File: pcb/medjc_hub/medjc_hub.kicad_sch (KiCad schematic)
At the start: 4 parts, among them J1 Barrel_Jack_Switch, U1 ESP32-C3_SUPERMINI, U2 MCP3208-CI_P, U3 NJM2747D

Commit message: 🚧 WIP: Kicad 回路図を更新
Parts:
- removed J1: Barrel_Jack_Switch, symbol Connector:Barrel_Jack_Switch
- removed U1: ESP32-C3_SUPERMINI, ESP32-C3_SUPERMINI:MODULE_ESP32-C3_SUPERMINI, symbol ESP32-C3_SUPERMINI:ESP32-C3_SUPERMINI
- added C1: 47μF, symbol Device:C_Polarized
- added C10, C12, C13, C14, C15, C4, C5, C6, C7, C8, C9: 0.1μF, symbol Device:C
- added C11, C2, C3: 0.47μF, symbol Device:C
- added D1: 1N4007, symbol Device:D
- added J1: Barrel_Jack, symbol Connector:Barrel_Jack
- added J2: Conn_01x02_Pin, Connector_PinHeader_2.54mm:PinHeader_1x02_P2.54mm_Vertical, symbol Connector:Conn_01x02_Pin
- added R1, R15, R2: 33kΩ, symbol Device:R
- added R10, R11, R12, R13, R14, R4, R5, R6, R7, R8, R9: 10kΩ, symbol Device:R
- added R3: 10kΩ, Resistor_THT:R_Box_L13.0mm_W4.0mm_P9.00mm, symbol Device:R
- added U1: NJU7223F33, symbol NJU7223F33:NJU7223F33
- added U3: ESP32-C3_SUPERMINI, ESP32-C3_SUPERMINI:MODULE_ESP32-C3_SUPERMINI, symbol ESP32-C3_SUPERMINI:ESP32-C3_SUPERMINI
- added U5, U6, U7: MERB-09, symbol MEDJC09:MERB-09
- renumbered U3 to U2, U2 to U4
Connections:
- net at U2.1 (OUT_A): now also R5.2, R6.2
- net at U2.10 (+IN_C): now also R11.1
- net GND: now reaches U2.11 (GND)
- net GND: now also U4.14 (AGND), U4.9 (DGND), C1.2, C10.2, C12.2, C13.2, C14.2, C15.2, C4.1, C5.2, C6.1, C7.2, C8.2, C9.1, J1.2, R1.1, R15.1, R2.2, U1.3 (GND), U3.G (GND), U5.3 (GND), U6.3 (GND), U7.3 (GND)
- net at U2.2 (-IN_A): now also R3.2, R6.1
- net at U2.3 (+IN_A): now also R9.2
- net +3V3: now reaches U2.4 (+Vin)
- net +3V3: now also U4.15 (VREF), U4.16 (VDD), U4.7 (CH6), C12.1, C13.1, C14.1, C15.1, C8.1, D1.1 (K), J2.2 (Pin_2), R10.2, R11.2, R9.1, U5.1 (Vs), U6.1 (Vs), U7.1 (Vs)
- net at U2.5 (+IN_B): now also R10.1
- net at U2.6 (-IN_B): now also R4.2, R7.1
- net at U2.7 (OUT_B): now also R7.2, R8.2
- net at U2.8 (OUT_C): now also R12.1, R13.1
- net at U2.9 (-IN_C): now also R13.2, R14.1
- net FME1: now reaches U4.1 (CH0)
- net FME1: now also C3.1, R1.2
- net SS: now reaches U4.10 (~CS/SHDN)
- net SS: now also U3.9 (GPIO9)
- net MOSI: now reaches U4.11 (DIN)
- net MOSI: now also U3.8 (GPIO8)
- net MISO: now reaches U4.12 (DOUT)
- net MISO: now also U3.7 (GPIO7)
- net SCK: now reaches U4.13 (CLK)
- net SCK: now also U3.4 (GPIO4)
- net SME1: now reaches U4.2 (CH1)
- net SME1: now also U5.5 (SME)
- net FME2: now reaches U4.3 (CH2)
- net FME2: now also C2.1, R2.1
- net SME2: now reaches U4.4 (CH3)
- net SME2: now also U6.5 (SME)
- net FME3: now reaches U4.5 (CH4)
- net FME3: now also C11.2, R15.2
- net SME3: now reaches U4.6 (CH5)
- net SME3: now also U7.5 (SME)
- new net: C10.1, J2.1 (Pin_1), U3.3.3 (3V3)
- new net: C1.1, C5.1, J1.1, U1.2 (Vin)
- new net: C2.2, C7.1, R8.1
- new net: C3.2, C6.2, R5.1
- new net: C4.2, D1.2 (A), U1.1 (Vout)
- new net: C11.1, C9.2, R12.2
- new net RAWME1: R3.1, U5.2 (ME)
- new net RAWME2: R4.1, U6.2 (ME)
- new net RAWME3: R14.2, U7.2 (ME)
- no-connect marks 0 -> 17
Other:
- moved on the sheet: U2, U4

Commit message: 📝 Update: 回路図を更新
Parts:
- removed C1: 47μF, symbol Device:C_Polarized
- removed C4: 0.1μF, symbol Device:C
- removed R10, R11, R9: 10kΩ, symbol Device:R
- removed U1: NJU7223F33, symbol NJU7223F33:NJU7223F33
- added C12, C6: 0.1μF, Capacitor_THT:C_Disc_D3.0mm_W2.0mm_P2.50mm, symbol Device:C
- added C4: 47μF, Capacitor_THT:CP_Radial_D5.0mm_P2.50mm, symbol Device:C_Polarized
- added J2, J3, J4: Conn_01x05_Socket, Connector_PinSocket_2.54mm:PinSocket_1x05_P2.54mm_Vertical, symbol Connector:Conn_01x05_Socket
- added J6, J7, J8: Conn_01x05_Pin, symbol Connector:Conn_01x05_Pin
- added R5: 10kΩ, Resistor_THT:R_Axial_DIN0207_L6.3mm_D2.5mm_P10.16mm_Horizontal, symbol Device:R
- added RV1: 5kΩ, GF063:GF063P, symbol Device:R_Potentiometer
- added U2: BA033CC0T, BA033CC0T:BA033CC0T, symbol BA033CC0T:BA033CC0T
- C1: renamed from C13; footprint (none) -> Capacitor_THT:C_Disc_D3.0mm_W2.0mm_P2.50mm
- C10: renamed from C6; value 0.1μF -> 1μF; footprint (none) -> Capacitor_THT:C_Disc_D3.0mm_W2.0mm_P2.50mm
- C11: renamed from C7; value 0.1μF -> 1μF; footprint (none) -> Capacitor_THT:C_Disc_D3.0mm_W2.0mm_P2.50mm
- C13: renamed from C8; footprint (none) -> Capacitor_THT:C_Disc_D3.0mm_W2.0mm_P2.50mm
- C14: renamed from C12; footprint (none) -> Capacitor_THT:C_Disc_D3.0mm_W2.0mm_P2.50mm
- C15: renamed from C9; value 0.1μF -> 1μF; footprint (none) -> Capacitor_THT:C_Disc_D3.0mm_W2.0mm_P2.50mm
- C16: renamed from C11; footprint (none) -> Capacitor_THT:C_Disc_D3.0mm_W2.0mm_P2.50mm
- C2: renamed from C14; footprint (none) -> Capacitor_THT:C_Disc_D3.0mm_W2.0mm_P2.50mm
- C3: renamed from C15; footprint (none) -> Capacitor_THT:C_Disc_D3.0mm_W2.0mm_P2.50mm
- C5: footprint (none) -> Capacitor_THT:C_Disc_D3.0mm_W2.0mm_P2.50mm
- C7: renamed from C10; footprint (none) -> Capacitor_THT:C_Disc_D3.0mm_W2.0mm_P2.50mm
- C8: renamed from C2; footprint (none) -> Capacitor_THT:C_Disc_D3.0mm_W2.0mm_P2.50mm
- C9: renamed from C3; footprint (none) -> Capacitor_THT:C_Disc_D3.0mm_W2.0mm_P2.50mm
- D1: footprint (none) -> Diode_THT:D_A-405_P10.16mm_Horizontal
- J1: value Barrel_Jack -> MJ-180P; footprint (none) -> Connector_BarrelJack:BarrelJack_Horizontal
- R1, R2, R4: footprint (none) -> Resistor_THT:R_Axial_DIN0207_L6.3mm_D2.5mm_P10.16mm_Horizontal
- R10: renamed from R12; value 10kΩ -> 200Ω; footprint (none) -> Resistor_THT:R_Axial_DIN0207_L6.3mm_D2.5mm_P10.16mm_Horizontal
- R11: renamed from R13; footprint (none) -> Resistor_THT:R_Axial_DIN0207_L6.3mm_D2.5mm_P10.16mm_Horizontal
- R12: renamed from R14; footprint (none) -> Resistor_THT:R_Axial_DIN0207_L6.3mm_D2.5mm_P10.16mm_Horizontal
- R13: renamed from R15; footprint (none) -> Resistor_THT:R_Axial_DIN0207_L6.3mm_D2.5mm_P10.16mm_Horizontal
- R3: footprint Resistor_THT:R_Box_L13.0mm_W4.0mm_P9.00mm -> Resistor_THT:R_Axial_DIN0207_L6.3mm_D2.5mm_P10.16mm_Horizontal
- R6: renamed from R5; value 10kΩ -> 200Ω; footprint (none) -> Resistor_THT:R_Axial_DIN0207_L6.3mm_D2.5mm_P10.16mm_Horizontal
- R7: renamed from R6; footprint (none) -> Resistor_THT:R_Axial_DIN0207_L6.3mm_D2.5mm_P10.16mm_Horizontal
- R8: renamed from R7; footprint (none) -> Resistor_THT:R_Axial_DIN0207_L6.3mm_D2.5mm_P10.16mm_Horizontal
- R9: renamed from R8; value 10kΩ -> 200Ω; footprint (none) -> Resistor_THT:R_Axial_DIN0207_L6.3mm_D2.5mm_P10.16mm_Horizontal
- U6: renamed from U2; footprint (none) -> Package_DIP:DIP-14_W7.62mm_Socket
- U7: renamed from U4; footprint MCP3208-CI_P:DIP254P762X432-16 -> Package_DIP:DIP-16_W7.62mm_Socket
- renumbered J2 to J5, U3 to U1, U5 to U3, U6 to U4, U7 to U5
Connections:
- net +3V3: now also J2.1 (Pin_1), J3.1 (Pin_1), J4.1 (Pin_1), R5.1; no longer U3.1 (Vs), U4.1 (Vs), U5.1 (Vs)
- net GND: now also C12.2, C4.2, C6.1, J2.3 (Pin_3), J3.3 (Pin_3), J4.3 (Pin_3), J6.3 (Pin_3), J7.3 (Pin_3), J8.3 (Pin_3), RV1.2, RV1.3, U2.2 (N.C./GND)
- net RAWME1: now also J2.2 (Pin_2); no longer U3.2 (ME)
- net RAWME2: now also J3.2 (Pin_2); no longer U4.2 (ME)
- net RAWME3: now also J4.2 (Pin_2); no longer U5.2 (ME)
- net SME1: now also J2.5 (Pin_5); no longer U3.5 (SME)
- net SME2: now also J3.5 (Pin_5); no longer U4.5 (SME)
- net SME3: now also J4.5 (Pin_5); no longer U5.5 (SME)
- net at U6.10 (+IN_C): now also U6.3 (+IN_A), U6.5 (+IN_B), C12.1, R5.2, RV1.1
- net at U4.4 (REF): now also J7.4 (Pin_4)
- net at U5.4 (REF): now also J8.4 (Pin_4)
- net at C5.1, J1.1: now also U2.1 (Vcc)
- net at D1.2 (A): now also C4.1, C6.2, U2.3 (OUT)
- net at U3.4 (REF): now also J6.4 (Pin_4)
- new net: J6.1 (Pin_1), J7.1 (Pin_1), J8.1 (Pin_1), U3.1 (Vs), U4.1 (Vs), U5.1 (Vs)
- new net: J7.2 (Pin_2), U4.2 (ME)
- new net: J7.5 (Pin_5), U4.5 (SME)
- new net: J8.2 (Pin_2), U5.2 (ME)
- new net: J8.5 (Pin_5), U5.5 (SME)
- new net: J6.2 (Pin_2), U3.2 (ME)
- new net: J6.5 (Pin_5), U3.5 (SME)
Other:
- moved on the sheet: C1, C10, C11, C13, C14, C15, C16, C2, C3, C7, C8, C9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

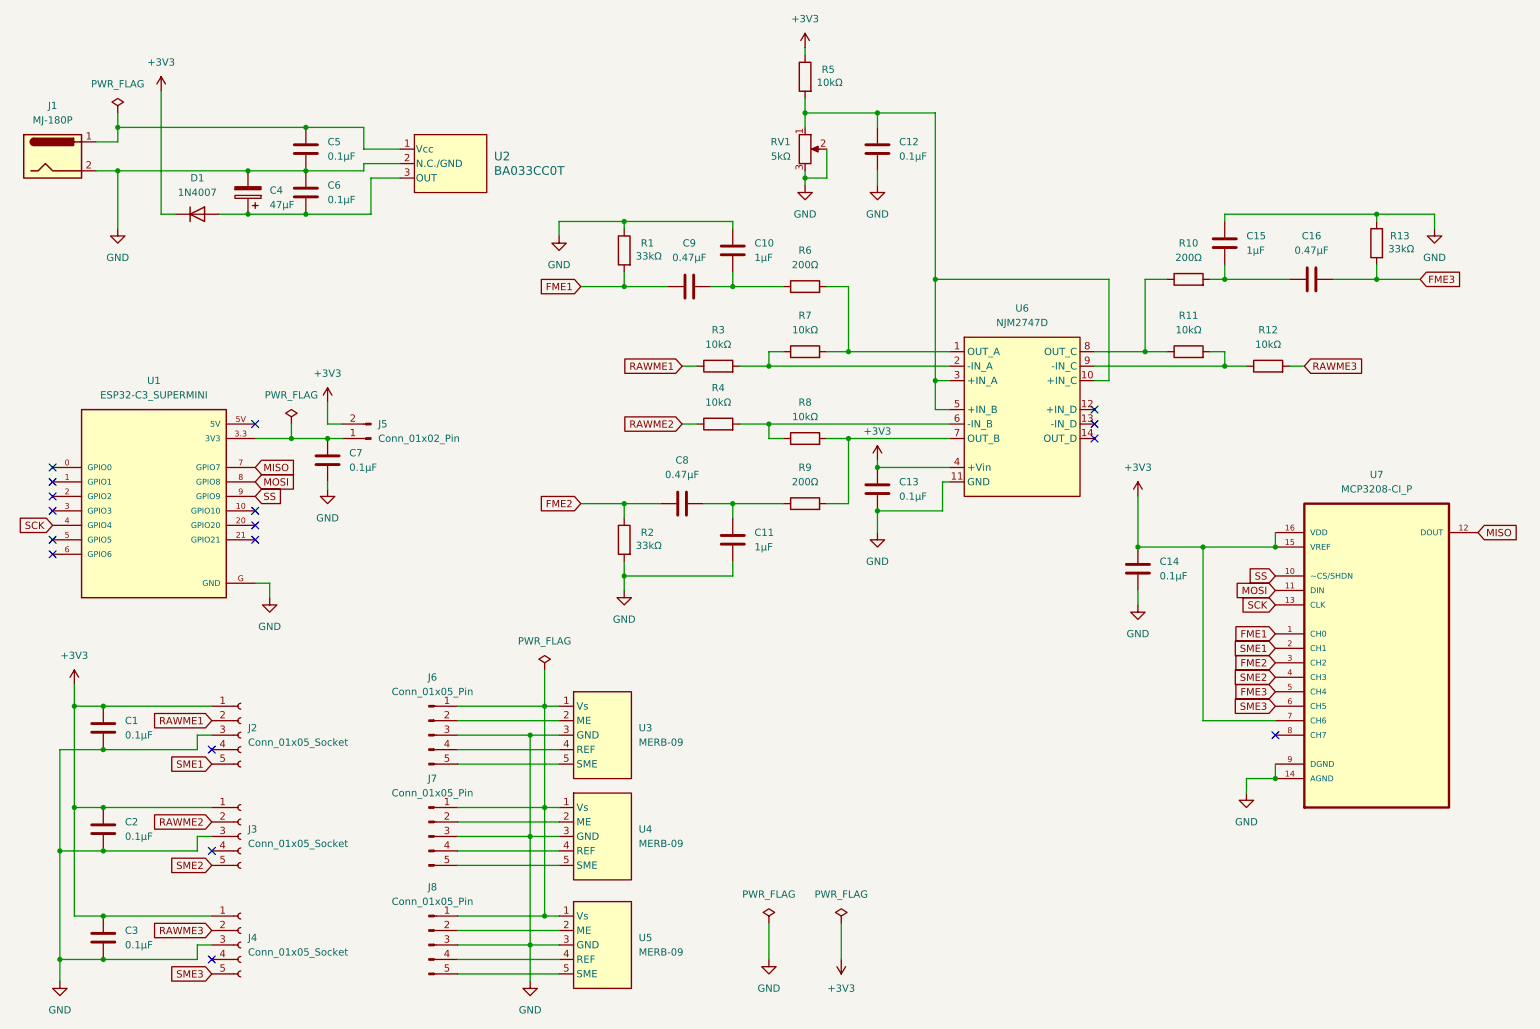
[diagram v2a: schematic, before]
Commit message: Update simulation waveform colors and add NJM2747D symbol library
- Changed the waveform color for the input voltage (VIN) to a new RGB value.
- Updated the waveform color for the output voltage (VOUT) to a different RGB value.
- Added cursor formatting for both VIN and VOUT signals in the simulation.
- Introduced a new symbol library for the NJM2747D component in the project.
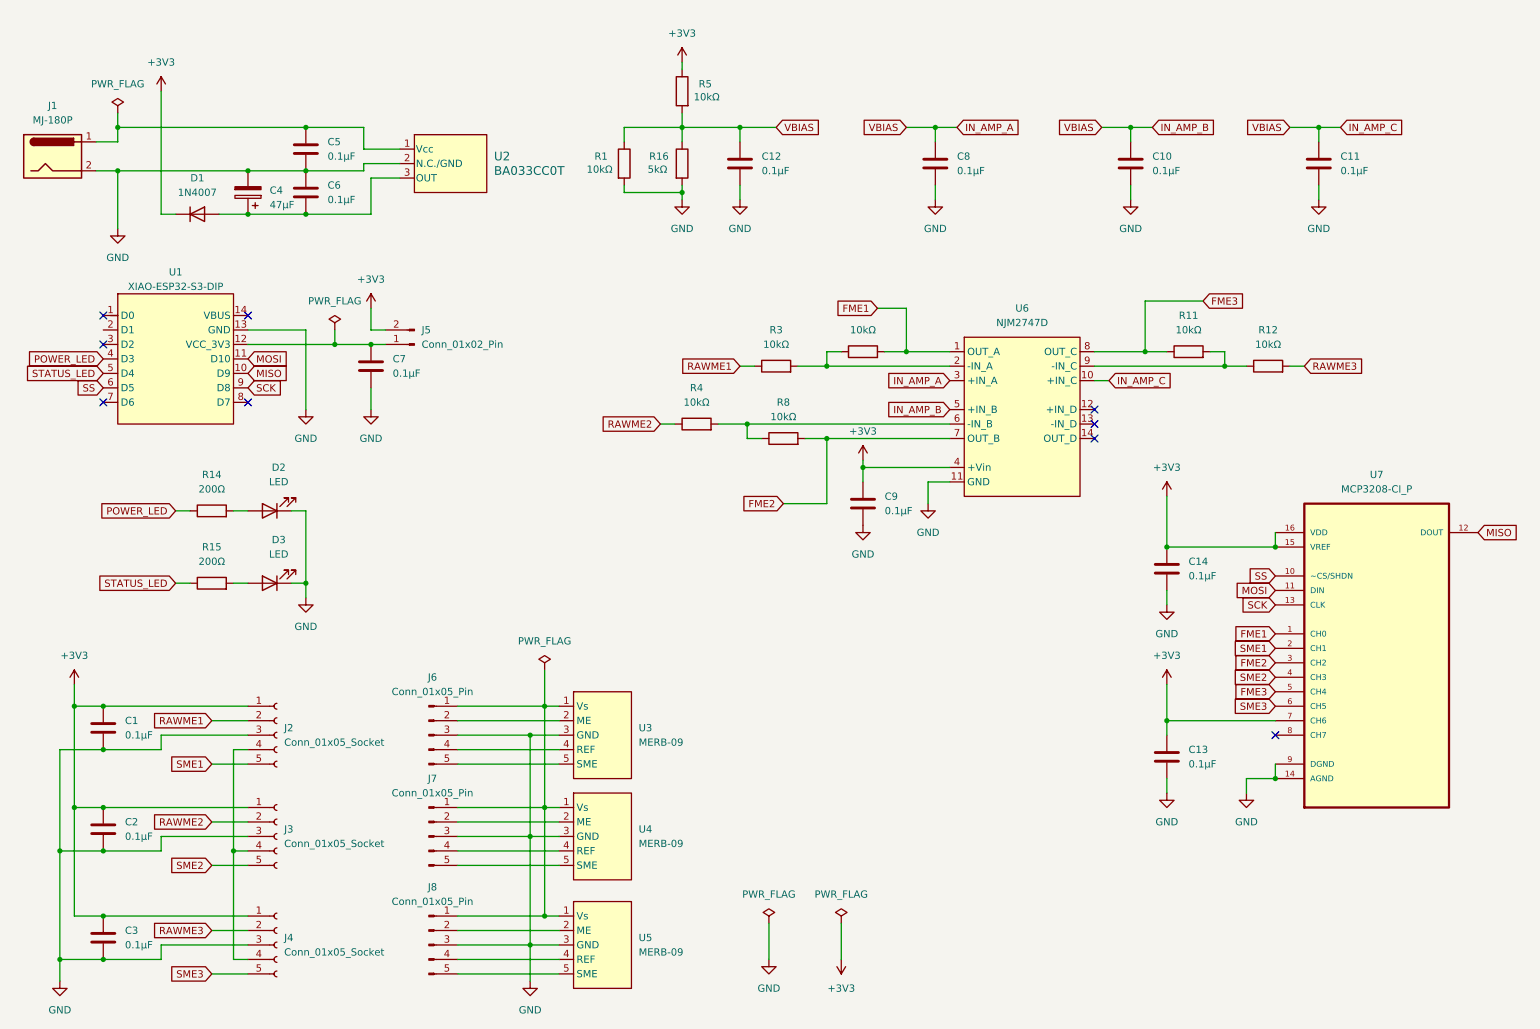
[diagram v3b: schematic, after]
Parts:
- removed C15: 1μF, Capacitor_THT:C_Disc_D3.0mm_W2.0mm_P2.50mm, symbol Device:C
- removed C16: 0.47μF, Capacitor_THT:C_Disc_D3.0mm_W2.0mm_P2.50mm, symbol Device:C
- removed R10, R6, R9: 200Ω, Resistor_THT:R_Axial_DIN0207_L6.3mm_D2.5mm_P10.16mm_Horizontal, symbol Device:R
- removed R13, R2: 33kΩ, Resistor_THT:R_Axial_DIN0207_L6.3mm_D2.5mm_P10.16mm_Horizontal, symbol Device:R
- removed RV1: 5kΩ, GF063:GF063P, symbol Device:R_Potentiometer
- removed U1: ESP32-C3_SUPERMINI, ESP32-C3_SUPERMINI:MODULE_ESP32-C3_SUPERMINI, symbol ESP32-C3_SUPERMINI:ESP32-C3_SUPERMINI
- added D2, D3: LED, symbol Device:LED
- added R14, R15: 200Ω, Resistor_THT:R_Axial_DIN0207_L6.3mm_D2.5mm_P10.16mm_Horizontal, symbol Device:R
- added R16: 5kΩ, Resistor_THT:R_Axial_DIN0207_L6.3mm_D2.5mm_P10.16mm_Horizontal, symbol Device:R
- added U1: XIAO-ESP32-S3-DIP, Seeed Studio XIAO Series Library:XIAO-ESP32S3-DIP, symbol Seeed_Studio_XIAO_Series:XIAO-ESP32-S3-DIP
- C10, C11: value 1μF -> 0.1μF
- C8, C9: value 0.47μF -> 0.1μF
- R1: value 33kΩ -> 10kΩ
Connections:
- net +3V3: now also C9.1
- net FME1: now also R7.2, U6.1 (OUT_A); no longer C9.1, R1.2
- net FME2: now also R8.2, U6.7 (OUT_B); no longer C8.1
- net FME3: now also R11.1, U6.8 (OUT_C)
- net GND: now also C10.2, C8.2, C9.2, R1.2, D2.1 (K), D3.1 (K), R16.2, U1.13 (GND); no longer C10.1, R1.1
- net MISO: now also U1.10 (D9)
- net MOSI: now also U1.11 (D10)
- net SCK: now also U1.9 (D8)
- net SS: now also U1.6 (D5)
- net IN_AMP_A: now reaches C12.1, R5.2, U6.10 (+IN_C), U6.3 (+IN_A), U6.5 (+IN_B)
- net IN_AMP_A: now also C10.1, C11.1, C8.1, R1.1, R16.1
- net at J3.4 (Pin_4): now also J2.4 (Pin_4), J4.4 (Pin_4)
- net at C7.1, J5.1 (Pin_1): now also U1.12 (VCC_3V3)
- new net: D2.2 (A), R14.2
- new net: D3.2 (A), R15.2
- new net POWER_LED: R14.1, U1.4 (D3)
- new net STATUS_LED: R15.1, U1.5 (D4)
- no-connect marks 17 -> 9
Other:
- moved on the sheet: C12, C14, C7, J2, J3, J4, J5, R3, R4, R5, R8

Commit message: 🍱 update: pcb v2
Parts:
- D2, D3: footprint (none) -> LED_THT:LED_D5.0mm
- renumbered C5 to C1, C14 to C10, C1 to C11, C13 to C12, C2 to C13, C3 to C14, C12 to C2, C8 to C3, C10 to C4, C11 to C5, C4 to C6, C6 to C7, C7 to C8, J5 to J2, J2 to J3, J6 to J4, J3 to J5, J7 to J6, J4 to J7, R5 to R1, R14 to R10, R15 to R11, R1 to R2, R16 to R3, R7 to R4, R11 to R5, R3 to R6, R12 to R7, R4 to R8, R8 to R9, U2 to U1, U1 to U2, U6 to U3, U7 to U4, U3 to U5, U4 to U6, U5 to U7
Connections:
- no-connect marks 9 -> 10
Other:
- moved on the sheet: U1
